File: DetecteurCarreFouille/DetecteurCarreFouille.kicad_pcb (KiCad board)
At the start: 2 copper layers, 30.5 x 62 mm, 10 parts, among them J1 Alim 5V, J2 ARIG Interf, J3 Screw_Terminal_01x04

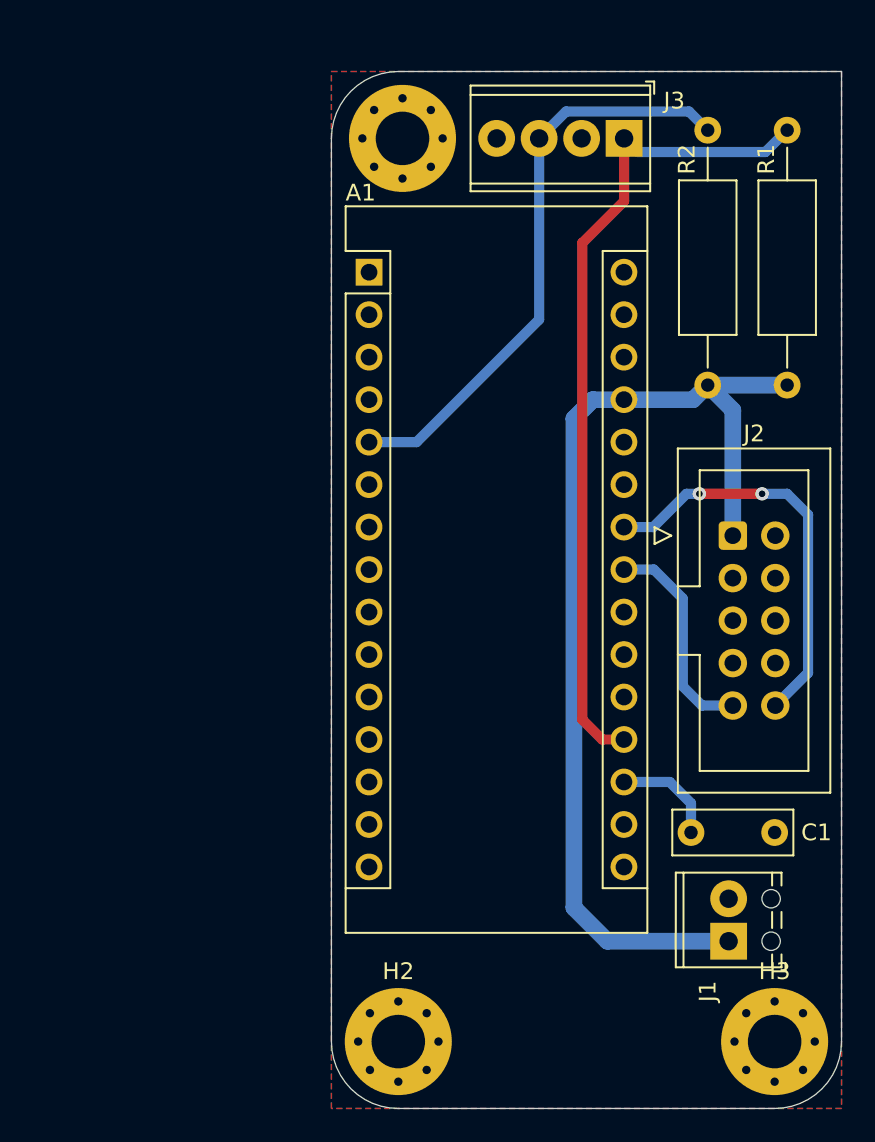
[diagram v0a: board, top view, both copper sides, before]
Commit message: Detecteur Carre fouille (pour 2022 en tous cas)
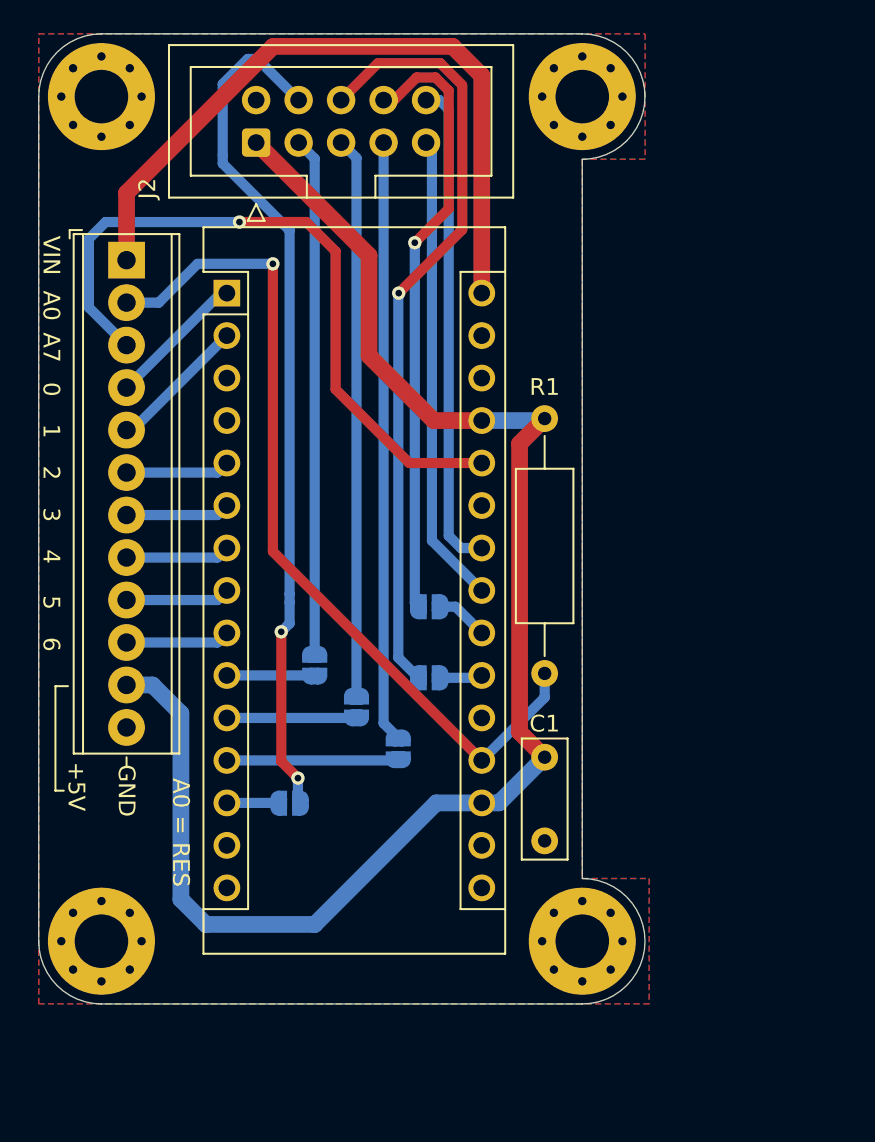
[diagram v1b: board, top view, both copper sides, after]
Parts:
- removed J1: Alim 5V, TerminalBlock_Phoenix:TerminalBlock_Phoenix_MPT-0,5-2-2.54_1x02_P2.54mm_Horizontal
- removed R2: 10k, Resistor_THT:R_Axial_DIN0309_L9.0mm_D3.2mm_P15.24mm_Horizontal
- added G***: LOGO, ARIG:Logo_ARIG_12_6x6_6, B.Cu at (113.0, 73.0)
- added H4: MountingHole_Pad, MountingHole:MountingHole_3.2mm_M3_Pad_Via, F.Cu at (129.2, 100.8)
- added JP1: SolderJumper_2_Open, Jumper:SolderJumper-2_P1.3mm_Open_RoundedPad1.0x1.5mm, B.Cu at (113.2, 84.2)
- added JP2: SolderJumper_2_Open, Jumper:SolderJumper-2_P1.3mm_Open_RoundedPad1.0x1.5mm, B.Cu at (111.8, 92.5)
- added JP3: SolderJumper_2_Open, Jumper:SolderJumper-2_P1.3mm_Open_RoundedPad1.0x1.5mm, B.Cu at (115.8, 86.8)
- added JP4: SolderJumper_2_Open, Jumper:SolderJumper-2_P1.3mm_Open_RoundedPad1.0x1.5mm, B.Cu at (120.1, 85.0)
- added JP5: SolderJumper_2_Open, Jumper:SolderJumper-2_P1.3mm_Open_RoundedPad1.0x1.5mm, B.Cu at (118.2, 89.2)
- added JP6: SolderJumper_2_Open, Jumper:SolderJumper-2_P1.3mm_Open_RoundedPad1.0x1.5mm, B.Cu at (120.1, 80.8)
- C1: footprint Capacitor_THT:C_Disc_D7.0mm_W2.5mm_P5.00mm -> Capacitor_THT:C_Rect_L7.0mm_W2.5mm_P5.00mm
- J3: value Screw_Terminal_01x04 -> Screw_Terminal_01x12; footprint TerminalBlock_Phoenix:TerminalBlock_Phoenix_MPT-0,5-4-2.54_1x04_P2.54mm_Horizontal -> TerminalBlock_Phoenix:TerminalBlock_Phoenix_MPT-0,5-12-2.54_1x12_P2.54mm_Horizontal
- moved H2 57.6 mm to (129.2, 50.2)
- moved H3 40.7 mm to (100.5, 100.8)
- moved J2 36.9 mm to (109.8, 53.0), turned to 90 degrees
- moved J3 30.6 mm to (102.0, 60.0), turned to -90 degrees
- moved H1 18.2 mm to (100.5, 50.2)
- moved R1 14.6 mm to (127.0, 69.5), turned to -90 degrees
- moved C1 9.84 mm to (127.0, 89.8), turned to -90 degrees
- moved A1 8.59 mm to (108.0, 62.0)
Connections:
- A1 pad 1: Net-(A1-Pad1) -> D0
- A1 pad 10: Net-(A1-Pad10) -> I3_U
- A1 pad 11: Net-(A1-Pad11) -> I5_U
- A1 pad 12: Net-(A1-Pad12) -> I7_U
- A1 pad 13: Net-(A1-Pad13) -> I4_U
- A1 pad 14: Net-(A1-Pad14) -> unconnected-(A1-Pad14)
- A1 pad 15: Net-(A1-Pad15) -> unconnected-(A1-Pad15)
- A1 pad 16: Net-(A1-Pad16) -> unconnected-(A1-Pad16)
- A1 pad 17: Net-(A1-Pad17) -> unconnected-(A1-Pad17)
- A1 pad 18: Net-(A1-Pad18) -> +5V
- A1 pad 2: Net-(A1-Pad2) -> D1
- A1 pad 20: Net-(A1-Pad20) -> unconnected-(A1-Pad20)
- A1 pad 21: Net-(A1-Pad21) -> I6_U
- A1 pad 22: Net-(A1-Pad22) -> I8_U
- A1 pad 25: Net-(A1-Pad25) -> unconnected-(A1-Pad25)
- A1 pad 26: Net-(A1-Pad26) -> A7
- A1 pad 28: Net-(A1-Pad28) -> unconnected-(A1-Pad28)
- A1 pad 3: Net-(A1-Pad3) -> unconnected-(A1-Pad3)
- A1 pad 30: Net-(A1-Pad30) -> VIN
- A1 pad 5: TOR -> D2
- A1 pad 6: Net-(A1-Pad6) -> D3
- A1 pad 7: Net-(A1-Pad7) -> D4
- A1 pad 8: Net-(A1-Pad8) -> D5
- A1 pad 9: Net-(A1-Pad9) -> D6
- C1 pad 1: Net-(A1-Pad18) -> +5V
- J2 pad 3: Net-(J2-Pad3) -> I3_C
- J2 pad 4: Net-(J2-Pad4) -> I4_C
- J2 pad 5: Net-(J2-Pad5) -> I5_C
- J2 pad 6: Net-(J2-Pad6) -> I6_C
- J2 pad 7: Net-(J2-Pad7) -> I7_C
- J2 pad 8: Net-(J2-Pad8) -> I8_C
- J3 pad 1: RES -> VIN
- J3 pad 2: GND -> RES
- J3 pad 3: TOR -> A7
- J3 pad 4: GND -> D0
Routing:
- net I4_C: track 0.00 -> 51.5 mm, vias 0 -> 2
- net I6_C: track 0.00 -> 46.1 mm, vias 0 -> 1
- net VIN: track 0.00 -> 42.6 mm
- net A7: track 0.00 -> 42.0 mm, vias 0 -> 1
- net I8_C: track 0.00 -> 36.6 mm, vias 0 -> 1
- net I7_C: track 0.00 -> 36.0 mm
- net TOR: track 35.2 -> 0.00 mm
- net I5_C: track 0.00 -> 33.5 mm
- net I3_C: track 0.00 -> 31.0 mm
- net +5V: track 62.5 -> 90.8 mm
- net SDA_5: track 13.0 -> 28.2 mm
- net I7_U: track 0.00 -> 10.3 mm
- net D0: track 0.00 -> 8.34 mm
- net D1: track 0.00 -> 8.34 mm
- net I5_U: track 0.00 -> 7.75 mm
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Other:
- board size 30.5 x 62 mm -> 36.2 x 58 mm
- net class Default removed
- board text added: "+5V"
- board text added: "0"
- board text added: "1"
- board text added: "2"
- board text added: "3"
- board text added: "4"
- board text added: "5"
- board text added: "6"
- board text added: "A0"
- board text added: "A0 = RES"
- board text added: "A7"
- board text added: "GND"
- board text added: "Interface Nano ARIG 2022"
- board text added: "VIN"
